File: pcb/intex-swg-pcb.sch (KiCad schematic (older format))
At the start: 8 parts, among them J1 230V, J2 Relay Board, J3 Display Board, J4 Main Board

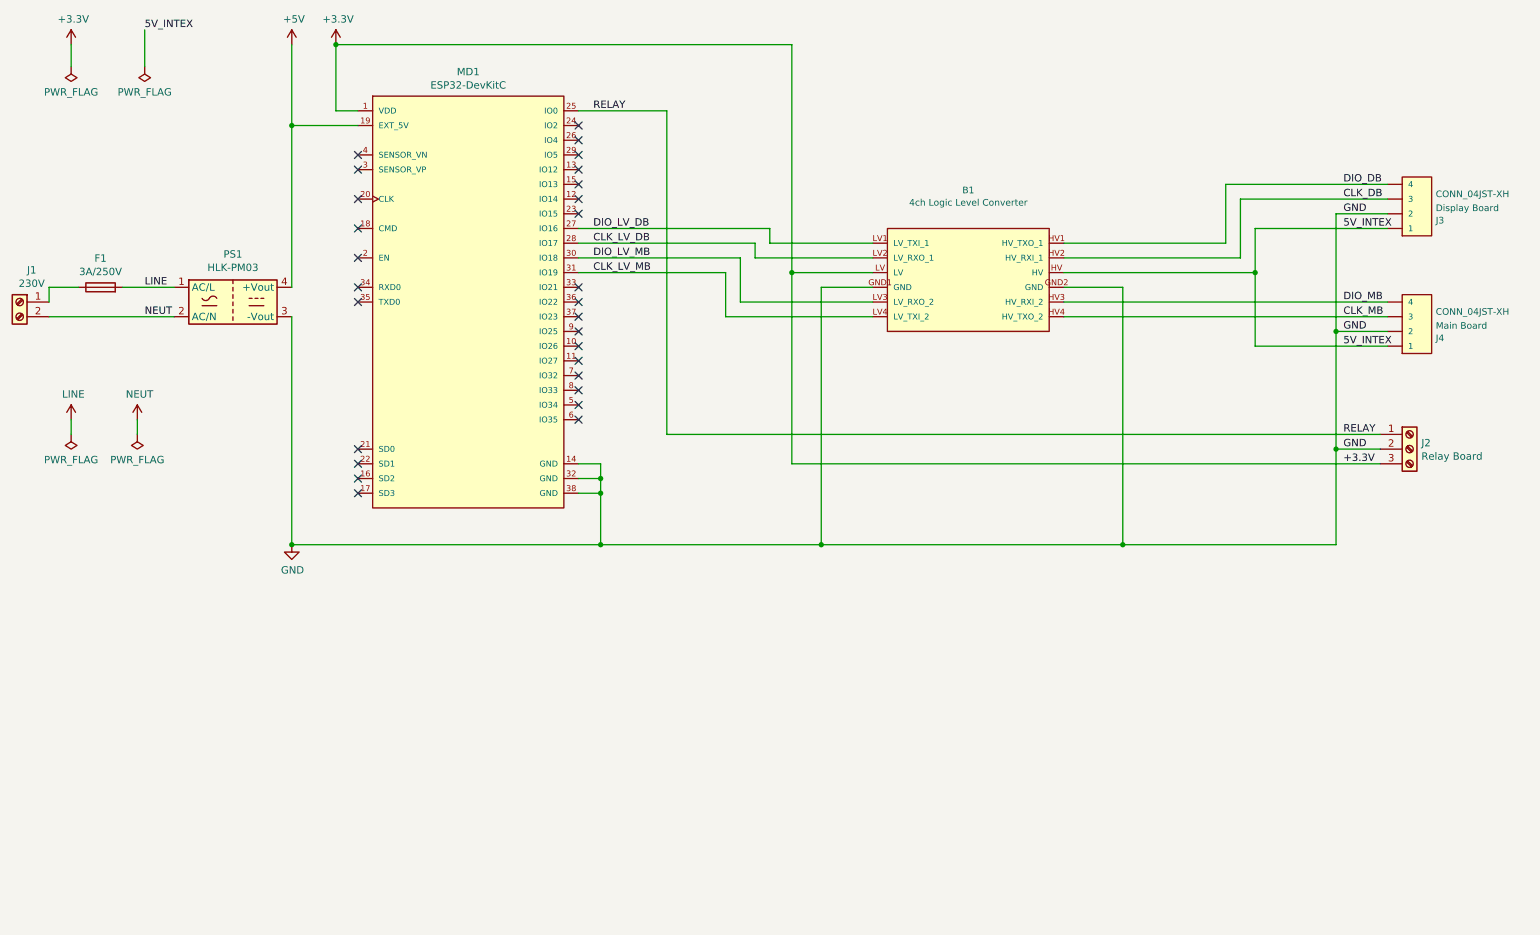
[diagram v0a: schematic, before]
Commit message: Swapped relay to GPIO2
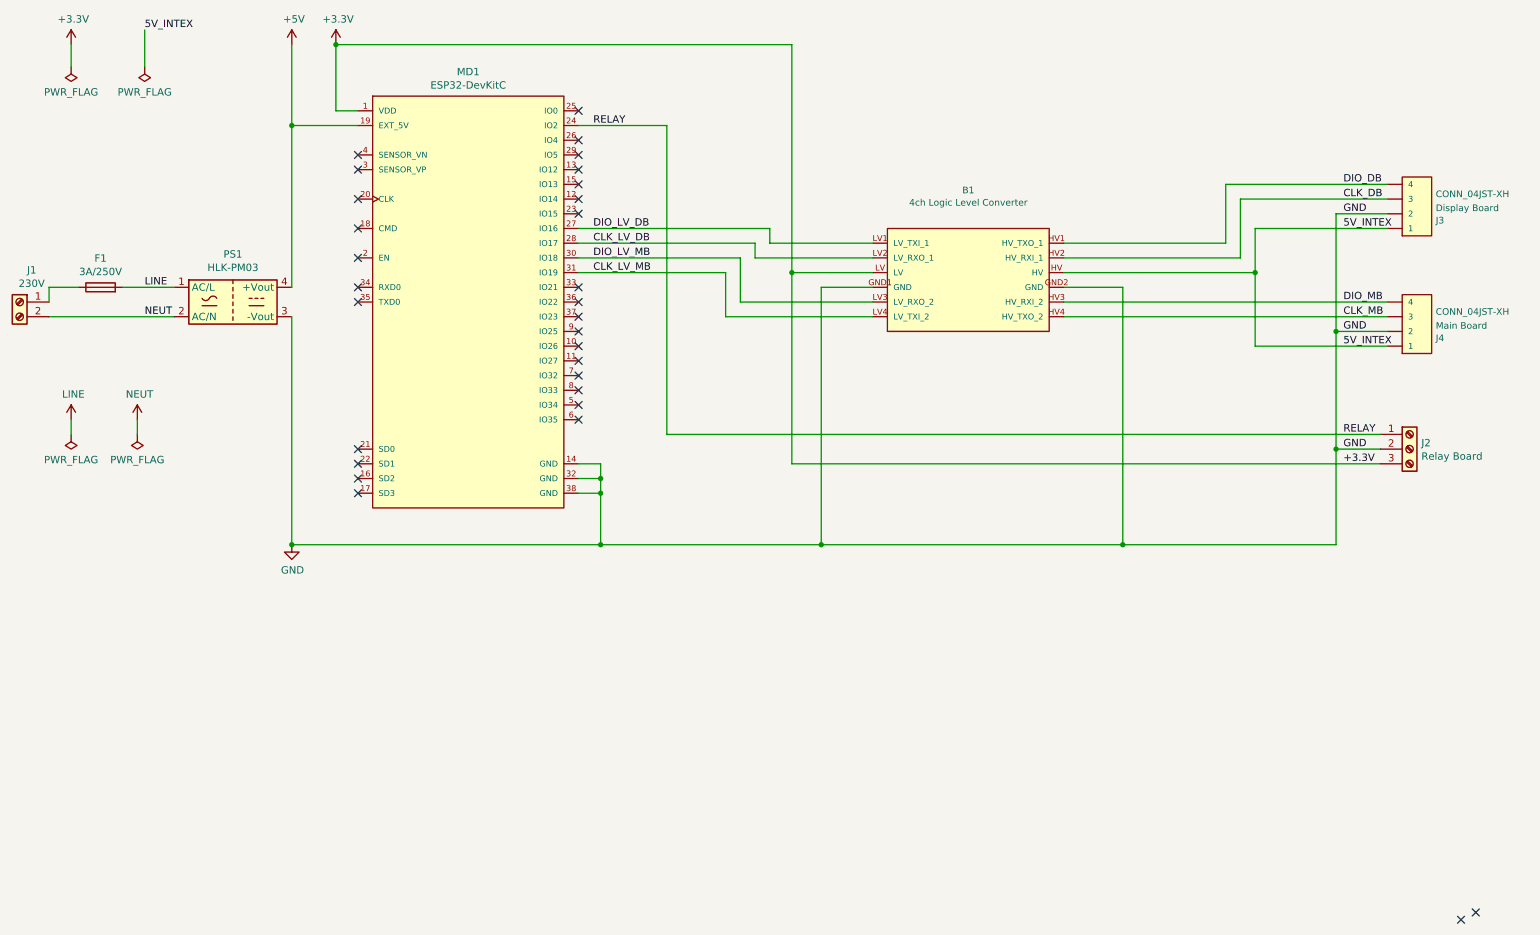
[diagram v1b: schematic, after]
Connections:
- net RELAY: now also MD1.24 (IO2); no longer MD1.25 (IO0)
- no-connect marks 28 -> 30
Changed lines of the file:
@@
 Sheet 1 1
 Title "Intex SWG w/TM1650 display board"
-Date "2022-05-22"
-Rev "2.0"
+Date "2022-06-11"
+Rev "2.1"
 Comp ""
 Comment1 ""
@@
 	10150 4500 6150 4500
 Wire Wire Line
-	5300 2100 5300 4300
-Wire Wire Line
-	5300 2100 4700 2100
+	5300 2200 5300 4300
 Wire Wire Line
 	4700 3000 5900 3000
@@
 Wire Wire Line
 	1100 3400 1100 3300
-NoConn ~ 4700 2200
 NoConn ~ 4700 2300
 NoConn ~ 4700 2400
@@
 Wire Wire Line
 	1750 1800 1750 1550
-Text Label 4800 2100 0    50   ~ 0
+Text Label 4800 2200 0    50   ~ 0
 RELAY
 Wire Wire Line
@@
 Wire Wire Line
 	9300 3700 10200 3700
+Wire Wire Line
+	5300 2200 4700 2200
+NoConn ~ 4700 2100
+NoConn ~ 10700 7600
+NoConn ~ 10800 7550
 $EndSCHEMATC
